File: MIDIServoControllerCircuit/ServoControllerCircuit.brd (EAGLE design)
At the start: 58.8 x 65.7 mm, 26 parts, among them Q1 20MHz, T1 2N3904, X1 SIGNAL-PWR-GND, X2 SIGNAL-PWR-GND

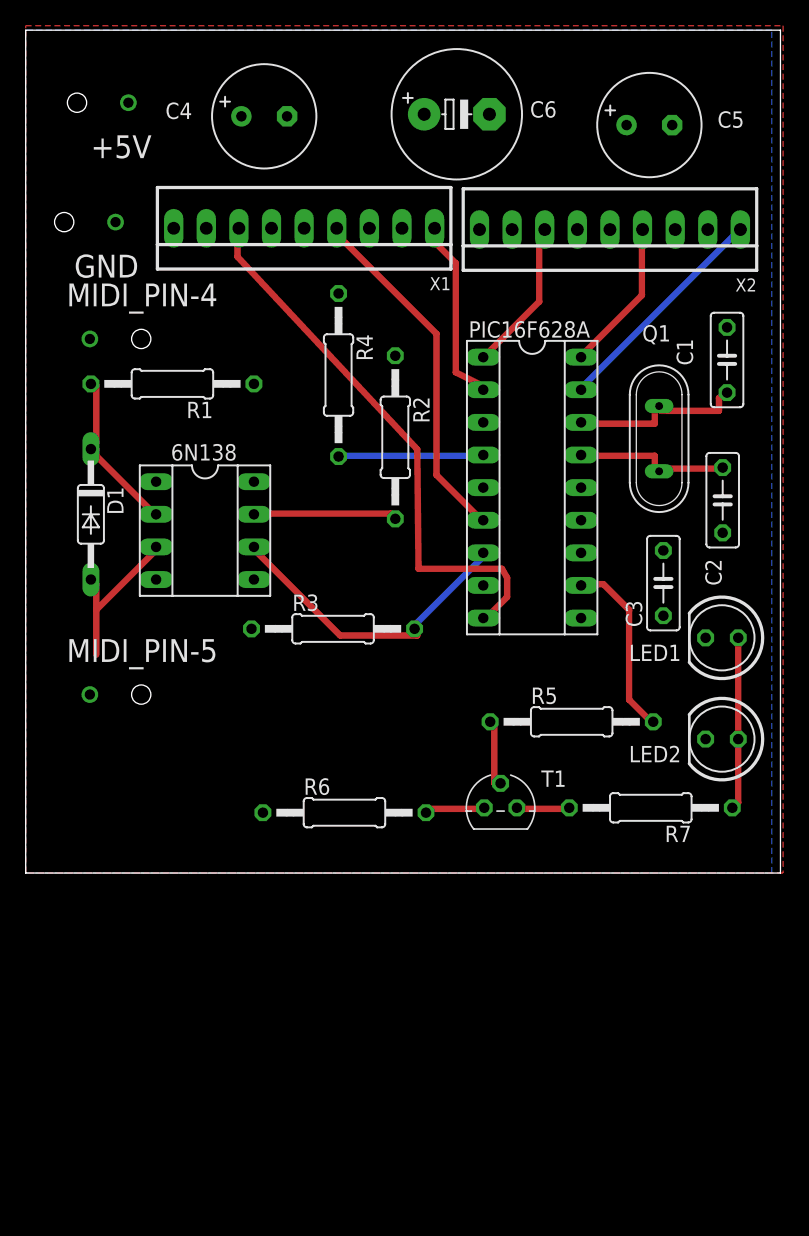
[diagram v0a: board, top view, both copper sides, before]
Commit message: Fixed LED directionality
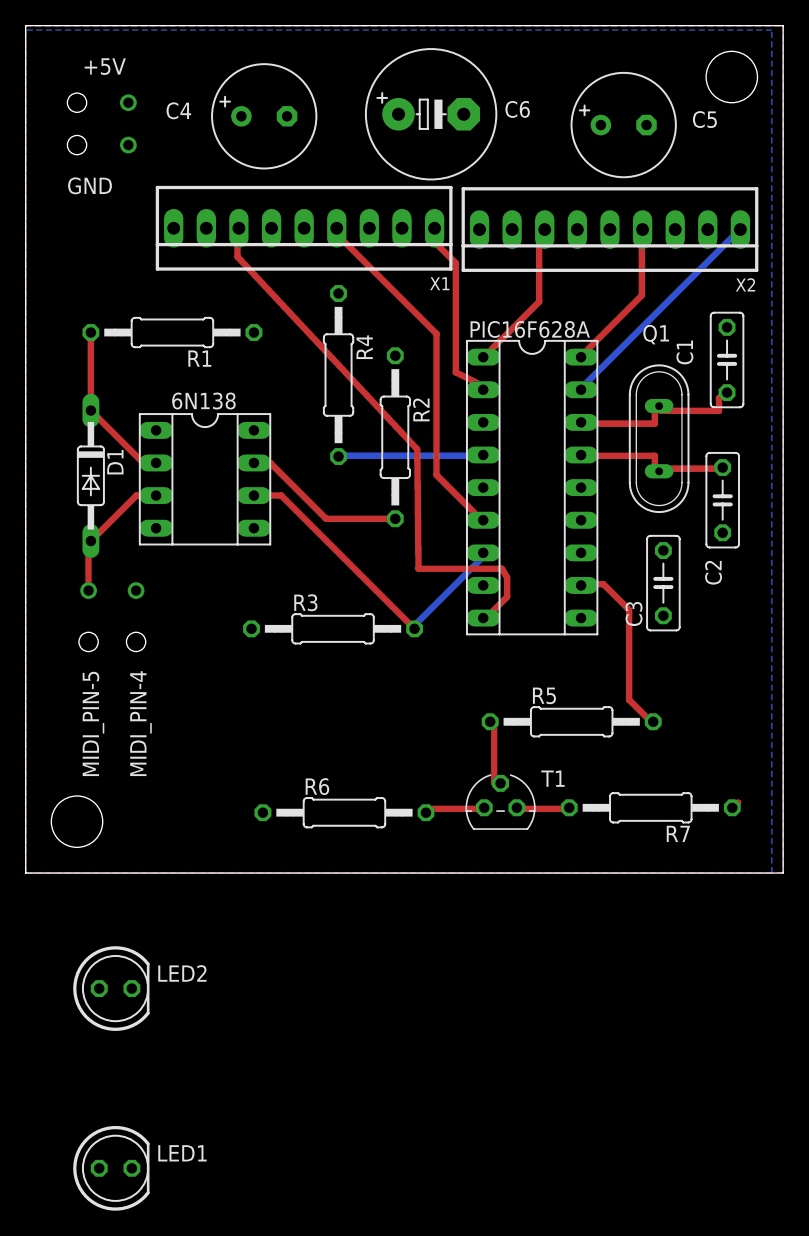
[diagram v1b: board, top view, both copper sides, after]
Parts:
- moved LED1 62.8 mm to (7.00, -23.0), turned to 0 degrees
- moved LED2 51.1 mm to (7.00, -9.00), turned to 0 degrees
- moved MIDI_PIN-4 21.7 mm to (8.60, 20.0), turned to 270 degrees
- moved MIDI_PIN-5 6.45 mm to (4.90, 20.0), turned to 270 degrees
- moved GND 6.08 mm to (6.00, 56.7)
- moved 6N138 4.00 mm to (14.0, 30.7)
- moved R1 4.00 mm to (11.4, 42.1)
- moved D1 3.00 mm to (5.08, 30.9)
- moved C5 2.00 mm to (46.6, 58.3)
- moved C6 2.00 mm to (31.6, 59.1)
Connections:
- net +5V: now also LED1.A, LED2.A; no longer LED1.K, LED2.K
- net N$10: now also LED1.K, LED2.K; no longer LED1.A, LED2.A
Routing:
- net N$10: track 13.4 -> 0.62 mm
- net MIDI_PIN-5: track 12.8 -> 10.5 mm
- net N$2: track 11.2 -> 12.8 mm
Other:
- board size 58.8 x 65.7 mm -> 59 x 66 mm

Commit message: Restored board layout
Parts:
- moved LED1 58.8 mm to (55.0, 11.0)
- moved LED2 55.1 mm to (55.0, 18.0)
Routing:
- net N$10: track 0.62 -> 14.1 mm
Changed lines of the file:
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@@
 <attribute name="NAME" x="4.44" y="15.81" size="1.27" layer="21" rot="R270"/>
 </element>
-<element name="LED2" library="led" library_urn="urn:adsk.eagle:library:259" package="LED5MM" package3d_urn="urn:adsk.eagle:package:15799/2" value="" x="7" y="-9"/>
-<element name="LED1" library="led" library_urn="urn:adsk.eagle:library:259" package="LED5MM" package3d_urn="urn:adsk.eagle:package:15799/2" value="" x="7" y="-23"/>
+<element name="LED2" library="led" library_urn="urn:adsk.eagle:library:259" package="LED5MM" package3d_urn="urn:adsk.eagle:package:15799/2" value="" x="55" y="18" smashed="yes">
+<attribute name="VALUE" x="58.2004" y="16.1966" size="1.27" layer="27" ratio="10"/>
+</element>
+<element name="LED1" library="led" library_urn="urn:adsk.eagle:library:259" package="LED5MM" package3d_urn="urn:adsk.eagle:package:15799/2" value="" x="55" y="11" smashed="yes">
+<attribute name="VALUE" x="58.2004" y="9.1966" size="1.27" layer="27" ratio="10"/>
+</element>
 </elements>
 <signals>
@@
 <contactref element="LED2" pad="A"/>
 <contactref element="LED1" pad="A"/>
-<wire x1="45.51" y1="50.12" x2="53.13" y2="50.12" width="0" layer="19" extent="1-1"/>
-<wire x1="37.89" y1="50.12" x2="45.51" y2="50.12" width="0" layer="19" extent="1-1"/>
-<wire x1="44.802" y1="58.26" x2="45.51" y2="50.12" width="0" layer="19" extent="1-1"/>
-<wire x1="29.31" y1="50.22" x2="37.89" y2="50.12" width="0" layer="19" extent="1-1"/>
-<wire x1="24.37" y1="45.14" x2="29.31" y2="50.22" width="0" layer="19" extent="1-1"/>
-<wire x1="21.69" y1="50.22" x2="24.37" y2="45.14" width="0" layer="19" extent="1-1"/>
-<wire x1="14.07" y1="50.22" x2="21.69" y2="50.22" width="0" layer="19" extent="1-1"/>
-<wire x1="29.04" y1="59.1" x2="29.31" y2="50.22" width="0" layer="19" extent="1-1"/>
-<wire x1="16.802" y1="58.94" x2="14.07" y2="50.22" width="0" layer="19" extent="1-1"/>
-<wire x1="8" y1="60" x2="16.802" y2="58.94" width="0" layer="19" extent="1-1"/>
-<wire x1="17.78" y1="34.48" x2="24.37" y2="45.14" width="0" layer="19" extent="1-1"/>
-<wire x1="17.59" y1="19.02" x2="17.78" y2="34.48" width="0" layer="19" extent="1-1"/>
-<wire x1="43.26" y1="30.02" x2="45.51" y2="50.12" width="0" layer="19" extent="1-1"/>
-<wire x1="49.67" y1="25.12" x2="43.26" y2="30.02" width="0" layer="19" extent="1-1"/>
-<wire x1="5.73" y1="-9" x2="17.59" y2="19.02" width="0" layer="19" extent="1-1"/>
-<wire x1="5.73" y1="-23" x2="5.73" y2="-9" width="0" layer="19" extent="1-1"/>
 </signal>
 <signal name="N$2">
@@
 <contactref element="LED2" pad="K"/>
 <contactref element="LED1" pad="K"/>
-<wire x1="8.27" y1="-9" x2="55.04" y2="5.08" width="0" layer="19" extent="1-1"/>
-<wire x1="8.27" y1="-23" x2="8.27" y2="-9" width="0" layer="19" extent="1-1"/>
+<wire x1="55.04" y1="5.08" x2="56.27" y2="6.31" width="0.5" layer="1"/>
+<wire x1="56.27" y1="6.31" x2="56.27" y2="11" width="0.5" layer="1"/>
+<wire x1="56.27" y1="11" x2="56.27" y2="18" width="0.5" layer="1"/>
 </signal>
 <signal name="N$6">

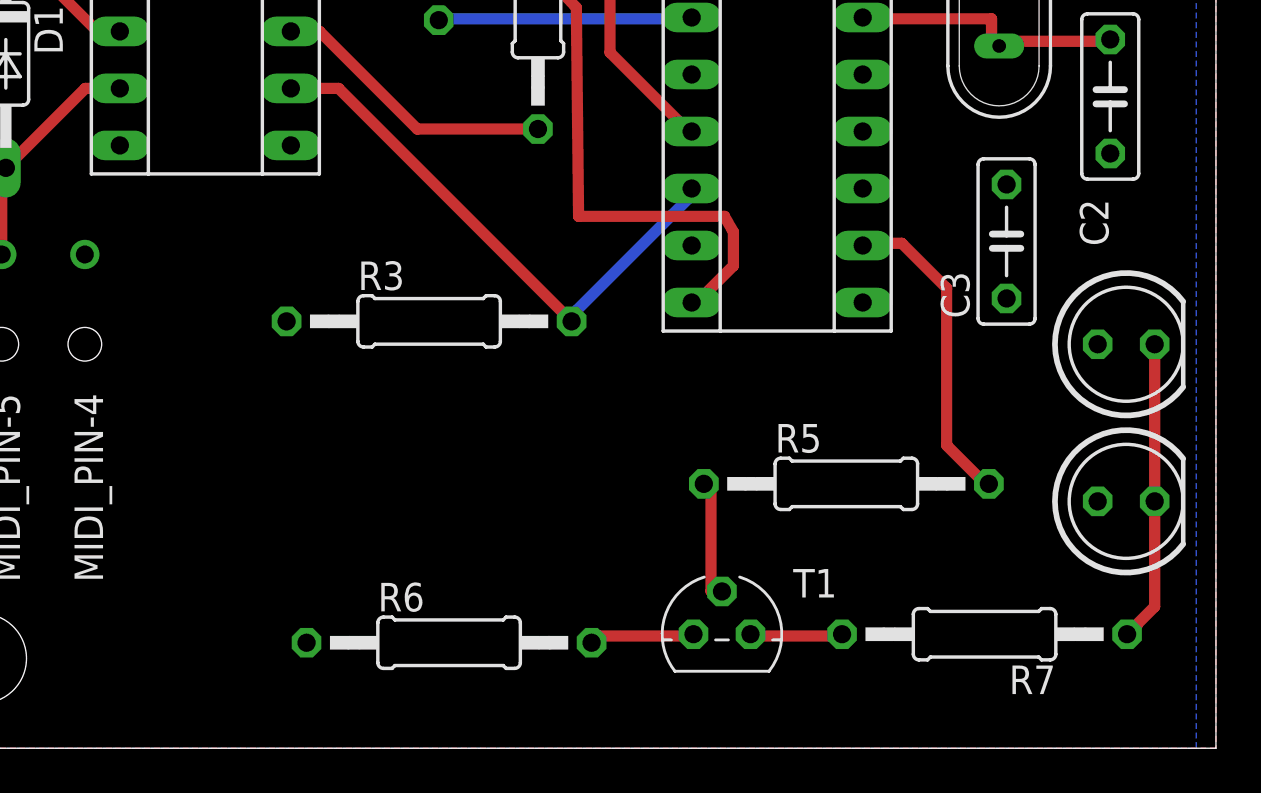
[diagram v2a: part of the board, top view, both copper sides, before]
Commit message: Added Remote LED component and updated board layout
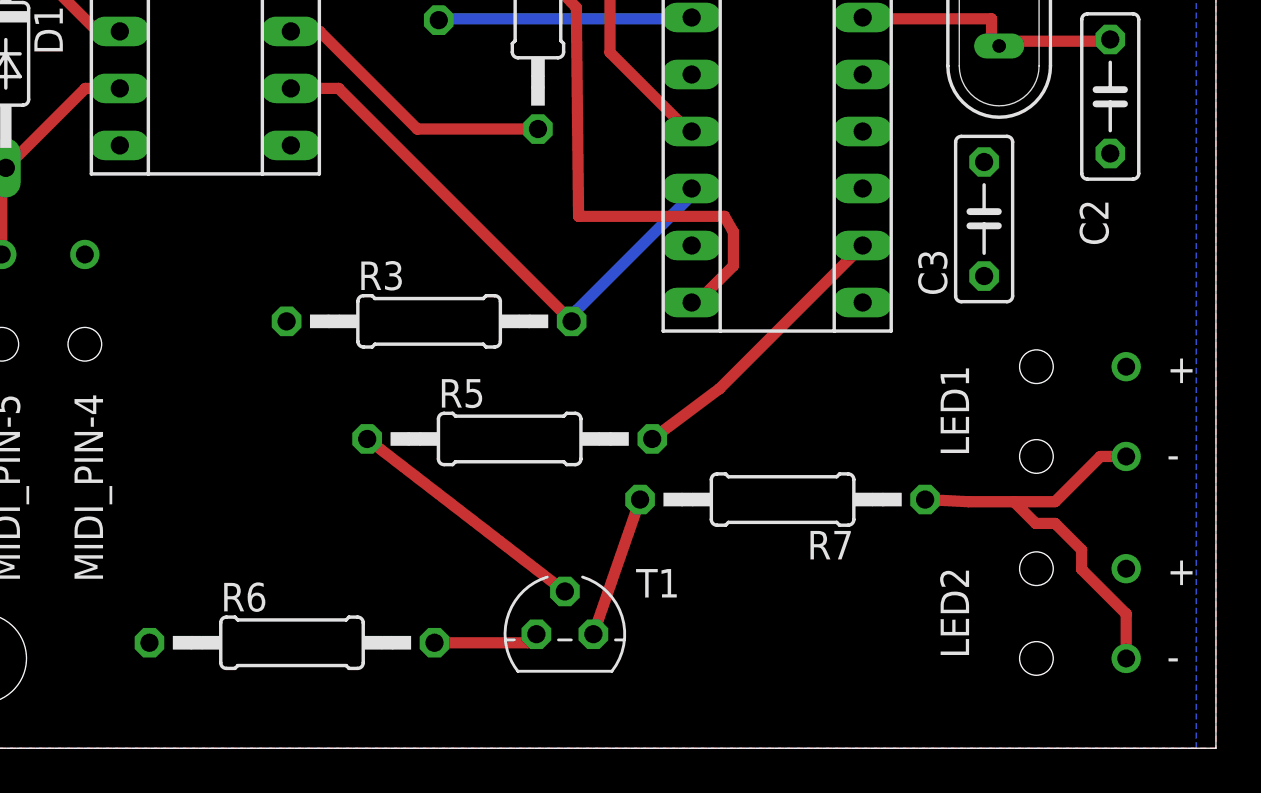
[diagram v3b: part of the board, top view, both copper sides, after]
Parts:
- LED1, LED2: value (none) -> REMOTE_LED; device led:LED5MM -> REMOTE_LED:REMOTE_LED
- moved R5 15.1 mm to (27.5, 13.8)
- moved LED2 12.2 mm to (53.0, 6.00)
- moved R7 10.8 mm to (39.7, 11.1)
- moved T1 7.00 mm to (30.0, 5.08)
- moved R6 7.00 mm to (17.8, 4.70)
- moved LED1 4.47 mm to (53.0, 15.0)
- moved C3 1.41 mm to (48.7, 23.6)
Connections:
- net +5V: now also LED1.P$1, LED2.P$1; no longer LED1.A, LED2.A
- net N$10: now also LED1.P$2, LED2.P$2; no longer LED1.K, LED2.K
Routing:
- net N$5: track 5.42 -> 11.1 mm
- net N$10: track 14.1 -> 19.4 mm
- net N$9: track 4.10 -> 6.35 mm
- net LIGHTS: track 14.1 -> 12.8 mm
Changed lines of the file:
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@@
 <attribute name="NAME" x="52.941" y="24.469" size="1.27" layer="25" ratio="10" rot="R270"/>
 </element>
-<element name="C3" library="resistor" library_urn="urn:adsk.eagle:library:348" package="C050-025X075" package3d_urn="urn:adsk.eagle:package:26160/1" value="0.1u" x="49.67" y="22.58" smashed="yes" rot="R90">
-<attribute name="NAME" x="48.019" y="19.151" size="1.27" layer="25" ratio="10" rot="R90"/>
+<element name="C3" library="resistor" library_urn="urn:adsk.eagle:library:348" package="C050-025X075" package3d_urn="urn:adsk.eagle:package:26160/1" value="0.1u" x="48.67" y="23.58" smashed="yes" rot="R90">
+<attribute name="NAME" x="47.019" y="20.151" size="1.27" layer="25" ratio="10" rot="R90"/>
 </element>
 <element name="C4" library="resistor" library_urn="urn:adsk.eagle:library:348" package="E3,5-8" package3d_urn="urn:adsk.eagle:package:25842/1" value="330uF" x="18.58" y="58.94" smashed="yes">
@@
 <attribute name="NAME" x="25.767" y="41.965" size="1.27" layer="25" ratio="10" rot="R270"/>
 </element>
-<element name="R5" library="resistor" library_urn="urn:adsk.eagle:library:348" package="0207/12" package3d_urn="urn:adsk.eagle:package:25938/1" value="1k" x="42.53" y="11.78" smashed="yes">
-<attribute name="NAME" x="39.355" y="13.177" size="1.27" layer="25" ratio="10"/>
-</element>
-<element name="R6" library="resistor" library_urn="urn:adsk.eagle:library:348" package="0207/12" package3d_urn="urn:adsk.eagle:package:25938/1" value="56" x="24.83" y="4.7" smashed="yes">
-<attribute name="NAME" x="21.655" y="6.097" size="1.27" layer="25" ratio="10"/>
-</element>
-<element name="R7" library="resistor" library_urn="urn:adsk.eagle:library:348" package="0207/12" package3d_urn="urn:adsk.eagle:package:25938/1" value="100" x="48.69" y="5.08" smashed="yes" rot="R180">
-<attribute name="NAME" x="51.865" y="3.683" size="1.27" layer="25" ratio="10" rot="R180"/>
-</element>
-<element name="T1" library="transistor" library_urn="urn:adsk.eagle:library:402" package="TO92" package3d_urn="urn:adsk.eagle:package:29893/2" value="2N3904" x="36.99" y="5.08" smashed="yes">
-<attribute name="NAME" x="40.165" y="6.715" size="1.27" layer="25" ratio="10"/>
+<element name="R5" library="resistor" library_urn="urn:adsk.eagle:library:348" package="0207/12" package3d_urn="urn:adsk.eagle:package:25938/1" value="1k" x="27.53" y="13.78" smashed="yes">
+<attribute name="NAME" x="24.355" y="15.177" size="1.27" layer="25" ratio="10"/>
+</element>
+<element name="R6" library="resistor" library_urn="urn:adsk.eagle:library:348" package="0207/12" package3d_urn="urn:adsk.eagle:package:25938/1" value="56" x="17.83" y="4.7" smashed="yes">
+<attribute name="NAME" x="14.655" y="6.097" size="1.27" layer="25" ratio="10"/>
+</element>
+<element name="R7" library="resistor" library_urn="urn:adsk.eagle:library:348" package="0207/12" package3d_urn="urn:adsk.eagle:package:25938/1" value="100" x="39.69" y="11.08" smashed="yes" rot="R180">
+<attribute name="NAME" x="42.865" y="9.683" size="1.27" layer="25" ratio="10" rot="R180"/>
+</element>
+<element name="T1" library="transistor" library_urn="urn:adsk.eagle:library:402" package="TO92" package3d_urn="urn:adsk.eagle:package:29893/2" value="2N3904" x="29.99" y="5.08" smashed="yes">
+<attribute name="NAME" x="33.165" y="6.715" size="1.27" layer="25" ratio="10"/>
 </element>
 <element name="X1" library="con-molex" library_urn="urn:adsk.eagle:library:165" package="22-23-2091" value="SIGNAL-PWR-GND" x="21.69" y="50.22" smashed="yes" rot="R180">
@@
 <attribute name="NAME" x="4.44" y="15.81" size="1.27" layer="21" rot="R270"/>
 </element>
-<element name="LED2" library="led" library_urn="urn:adsk.eagle:library:259" package="LED5MM" package3d_urn="urn:adsk.eagle:package:15799/2" value="" x="55" y="18" smashed="yes">
-<attribute name="VALUE" x="58.2004" y="16.1966" size="1.27" layer="27" ratio="10"/>
-</element>
-<element name="LED1" library="led" library_urn="urn:adsk.eagle:library:259" package="LED5MM" package3d_urn="urn:adsk.eagle:package:15799/2" value="" x="55" y="11" smashed="yes">
-<attribute name="VALUE" x="58.2004" y="9.1966" size="1.27" layer="27" ratio="10"/>
+<element name="LED1" library="REMOTE_LED" package="REMOTE_LED" value="REMOTE_LED" x="53" y="15" smashed="yes">
+<attribute name="NAME" x="48" y="13" size="1.27" layer="21" rot="R90"/>
+</element>
+<element name="LED2" library="REMOTE_LED" package="REMOTE_LED" value="REMOTE_LED" x="53" y="6" smashed="yes">
+<attribute name="NAME" x="48" y="4" size="1.27" layer="21" rot="R90"/>
 </element>
 </elements>
@@
 </polygon>
 <contactref element="+5V" pad="P$1"/>
-<contactref element="LED2" pad="A"/>
-<contactref element="LED1" pad="A"/>
+<contactref element="LED1" pad="P$1"/>
+<contactref element="LED2" pad="P$1"/>
 </signal>
 <signal name="N$2">
@@
 <contactref element="PIC16F628A" pad="11"/>
 <contactref element="R5" pad="2"/>
-<wire x1="47" y1="13.5" x2="48.5" y2="12" width="0.5" layer="1"/>
-<wire x1="47" y1="20.5" x2="47" y2="13.5" width="0.5" layer="1"/>
-<wire x1="45" y1="22.5" x2="47" y2="20.5" width="0.5" layer="1"/>
-<wire x1="43.5" y1="22.5" x2="45" y2="22.5" width="0.5" layer="1"/>
-<wire x1="48.5" y1="12" x2="48.88" y2="11.78" width="0.5" layer="1"/>
-<wire x1="43.5" y1="22.5" x2="43.26" y2="22.4" width="0.5" layer="1"/>
+<wire x1="33.88" y1="13.78" x2="36.88" y2="16.02" width="0.5" layer="1"/>
+<wire x1="36.88" y1="16.02" x2="43.26" y2="22.4" width="0.5" layer="1"/>
 </signal>
 <signal name="N$5">
 <contactref element="R5" pad="1"/>
 <contactref element="T1" pad="2"/>
-<wire x1="36.5" y1="11.5" x2="36.5" y2="7" width="0.5" layer="1"/>
-<wire x1="36.5" y1="7" x2="36.99" y2="6.985" width="0.5" layer="1"/>
-<wire x1="36.5" y1="11.5" x2="36.18" y2="11.78" width="0.5" layer="1"/>
+<wire x1="29.99" y1="6.985" x2="21.18" y2="13.78" width="0.5" layer="1"/>
 </signal>
 <signal name="N$7">
 <contactref element="R6" pad="2"/>
 <contactref element="T1" pad="3"/>
-<wire x1="35.5" y1="5" x2="31.5" y2="5" width="0.5" layer="1"/>
-<wire x1="31.5" y1="5" x2="31.18" y2="4.7" width="0.5" layer="1"/>
-<wire x1="35.5" y1="5" x2="35.72" y2="5.08" width="0.5" layer="1"/>
+<wire x1="24.18" y1="4.7" x2="28.34" y2="4.7" width="0.5" layer="1"/>
+<wire x1="28.34" y1="4.7" x2="28.72" y2="5.08" width="0.5" layer="1"/>
 </signal>
 <signal name="N$9">
 <contactref element="R7" pad="2"/>
 <contactref element="T1" pad="1"/>
-<wire x1="42" y1="5" x2="38.5" y2="5" width="0.5" layer="1"/>
-<wire x1="38.5" y1="5" x2="38.26" y2="5.08" width="0.5" layer="1"/>
-<wire x1="42" y1="5" x2="42.34" y2="5.08" width="0.5" layer="1"/>
+<wire x1="31.26" y1="5.08" x2="33.34" y2="11.08" width="0.5" layer="1"/>
 </signal>
 <signal name="N$10">
 <contactref element="R7" pad="1"/>
-<wire x1="55.5" y1="5.5" x2="55.04" y2="5.08" width="0.5" layer="1"/>
-<contactref element="LED2" pad="K"/>
-<contactref element="LED1" pad="K"/>
-<wire x1="55.04" y1="5.08" x2="56.27" y2="6.31" width="0.5" layer="1"/>
-<wire x1="56.27" y1="6.31" x2="56.27" y2="11" width="0.5" layer="1"/>
-<wire x1="56.27" y1="11" x2="56.27" y2="18" width="0.5" layer="1"/>
+<contactref element="LED1" pad="P$2"/>
+<contactref element="LED2" pad="P$2"/>
+<wire x1="53.85105625" y1="13" x2="55" y2="13" width="0.5" layer="1"/>
+<wire x1="51.83505625" y1="10.984" x2="53.85105625" y2="13" width="0.5" layer="1"/>
+<wire x1="46.04" y1="11.08" x2="47.976" y2="10.984" width="0.5" layer="1"/>
+<wire x1="47.976" y1="10.984" x2="50" y2="10.984" width="0.5" layer="1"/>
+<wire x1="50" y1="10.984" x2="51.83505625" y2="10.984" width="0.5" layer="1"/>
+<wire x1="55" y1="4" x2="55" y2="5.984" width="0.5" layer="1"/>
+<wire x1="55" y1="5.984" x2="53.016" y2="7.968" width="0.5" layer="1"/>
+<wire x1="53.016" y1="7.968" x2="53.016" y2="8.83505625" width="0.5" layer="1"/>
+<wire x1="53.016" y1="8.83505625" x2="51.83505625" y2="10.016" width="0.5" layer="1"/>
+<wire x1="51.83505625" y1="10.016" x2="50.968" y2="10.016" width="0.5" layer="1"/>
+<wire x1="50.968" y1="10.016" x2="50" y2="10.984" width="0.5" layer="1"/>
 </signal>
 <signal name="N$6">
